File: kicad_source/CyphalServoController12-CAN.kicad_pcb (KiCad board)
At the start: 2 copper layers, 81 x 57 mm, 94 parts, among them CN1 SM04B-SRSS-TB, CN10 GH_SM04B-GHS-TB, CN11 GH_SM04B-GHS-TB, CN12 Powerpole_2, CN13 DNI, CN14 DNI, CN2 CONN_02X03, CN3 CONN_02X03, CN4 CONN_02X03, CN5 CONN_02X03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

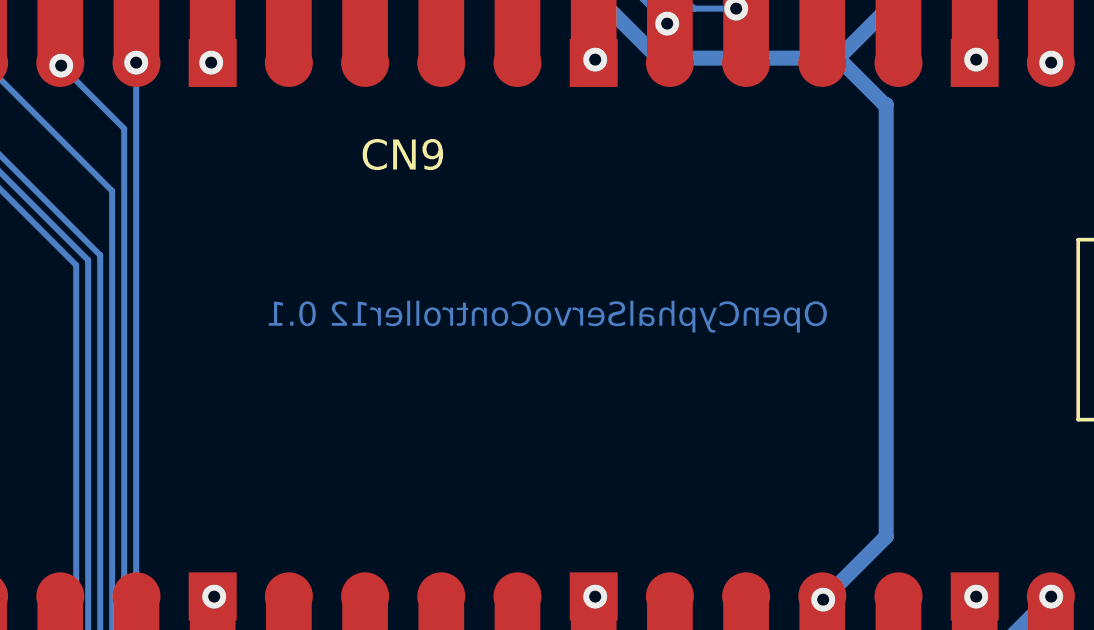
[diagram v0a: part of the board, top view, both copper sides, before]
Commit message: renamed comments and labels in kicad project
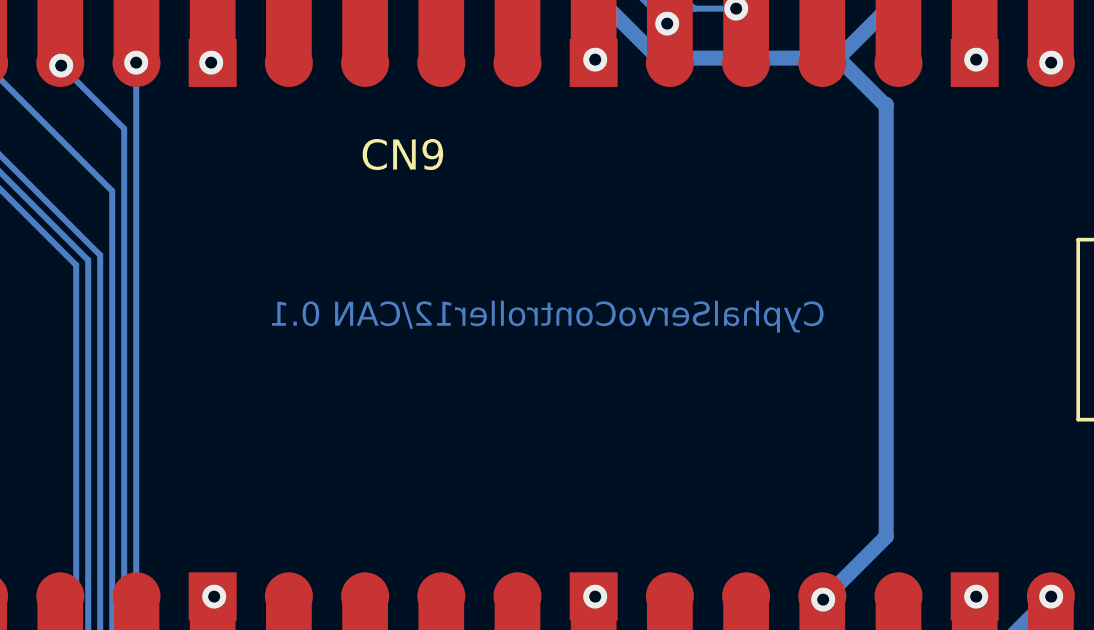
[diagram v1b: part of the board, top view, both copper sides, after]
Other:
- board text added: "CyphalServoController12/CAN 0.1"
- board text added: "find data and documentation at https://github.com/generationmake/CyphalServoController12-CAN"
- board text removed: "OpenCyphalServoController12 0.1"
- board text removed: "find data and documentation at https://github.com/generationmake/OpenCyphalServoController12"
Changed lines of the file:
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@@
   (paper "A4")
   (title_block
-    (title "OpenCyphalServoController12")
-    (date "2023-03-27")
+    (title "CyphalServoController12/CAN")
+    (date "2023-09-24")
     (rev "0.1")
     (company "generationmake")
@@
     (effects (font (size 1.5 1.5) (thickness 0.375)))
   )
-  (gr_text "OpenCyphalServoController12 0.1" (at 121.3 81) (layer "B.Cu")
+  (gr_text "CyphalServoController12/CAN 0.1" (at 121.3 81) (layer "B.Cu")
     (effects (font (size 0.8 0.8) (thickness 0.2)) (justify mirror))
   )
@@
     (effects (font (size 0.6 0.6) (thickness 0.15)) (justify left mirror))
   )
-  (gr_text "find data and documentation at\nhttps://github.com/generationmake/OpenCyphalServoController12" (at 139.7 87) (layer "B.SilkS")
+  (gr_text "find data and documentation at\nhttps://github.com/generationmake/CyphalServoController12-CAN" (at 139.7 87) (layer "B.SilkS")
     (effects (font (size 0.6 0.6) (thickness 0.15)) (justify left mirror))
   )
